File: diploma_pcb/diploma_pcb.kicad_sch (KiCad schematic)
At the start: 22 parts, among them Q1 2SC3356, Q3 2SC3356

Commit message: Divided in files, not made the showcase of the number
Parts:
- R1: value 2k -> 1k
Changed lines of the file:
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@@
 			)
 		)
-		(property "Value" "2k"
+		(property "Value" "1k"
 			(at 45.72 31.242 0)
 			(effects

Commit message: changes to ard, file button reader
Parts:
- Q1, Q3: footprint 2SC3356:SOT-23_MINIMOLD_REN -> 2SC3356:SOT-23_MINIMOLD_REN-M
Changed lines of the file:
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@@
 		)
 		(instances
-			(project ""
+			(project "diploma_pcb"
 				(path "/8eade999-89f4-4618-aeea-e9238b0bd165"
 					(reference "LED1")
@@
 			)
 		)
-		(property "Footprint" "2SC3356:SOT-23_MINIMOLD_REN"
+		(property "Footprint" "2SC3356:SOT-23_MINIMOLD_REN-M"
 			(at 48.895 62.865 0)
 			(effects
@@
 			)
 		)
-		(property "Footprint" "2SC3356:SOT-23_MINIMOLD_REN"
+		(property "Footprint" "2SC3356:SOT-23_MINIMOLD_REN-M"
 			(at 48.895 62.865 0)
 			(effects

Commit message: mods on PCB, Matplot, ?ard?
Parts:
- removed Q1, Q3: 2SC3356, 2SC3356:SOT-23_MINIMOLD_REN-M, symbol 2024-08-01_13-32-15:2SC3356
- removed R1: 1k, Resistor_SMD:R_1206_3216Metric, symbol Device:R
- removed R_3V3, R_5V1, R_div1, R_div2: R, Resistor_SMD:R_1206_3216Metric, symbol Device:R
- added C_oscilato1, C_supply1: .1uF, Capacitor_SMD:C_1206_3216Metric_Pad1.33x1.80mm_HandSolder, symbol Device:C
- added D1, D2: D_Schottky, symbol Device:D_Schottky
- added Q1: 2n3904, symbol Transistor_BJT:BC107
- added Rsch1: 1M, Resistor_SMD:R_1206_3216Metric, symbol Device:R
- R_gnd1, Rcc1: value 3k -> 4.7k
- Rf1: value 510к -> 680k
- Rg1: value 15к -> 10k
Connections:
- net Supply is gone; now on net 5V: 5_pins_op_amp1.5 (VDD), 8_pin_op_amp1.7 (V+), C1.1, C_GND1.2, Rcc1.1
- net 5V: now also D1.2 (A)
- net GND: now also C_supply1.1, Q1.2 (B)
- net Vout: now also A1.19 (A0)
- net at C104.1: now also Rsch1.2
- net at A1.14 (MOSI): now also C_oscilato1.2
- net 3.3V: no longer names the net of A1.17 (3V3)
- net signal renamed Signal
- new net: C_supply1.2, D1.1 (K), D2.1 (K), Q1.1 (E), Rsch1.1
- new net: C_oscilato1.1, D2.2 (A)
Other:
- note removed: "2SC3356"
- moved on the sheet: C104, C_GND1, R_gnd1, Rcc1

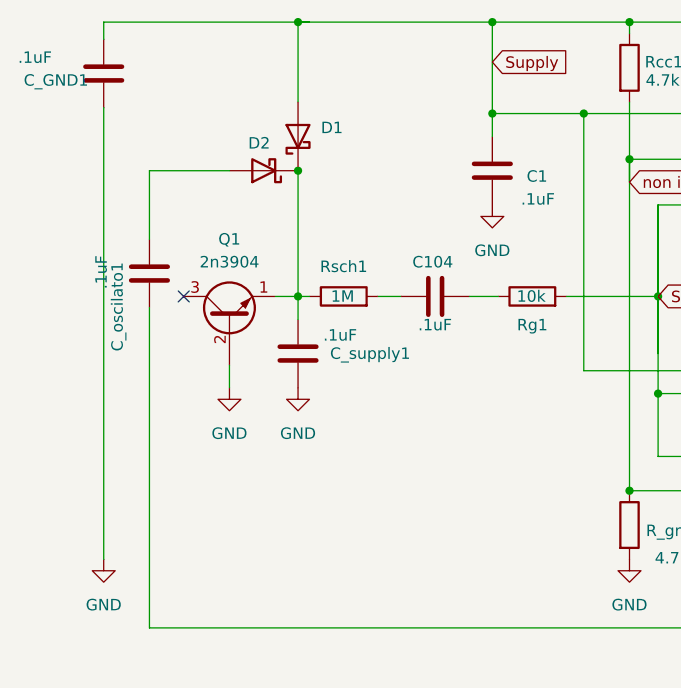
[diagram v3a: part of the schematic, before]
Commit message: PCB fixed Schottkey, Ard code with Union, GNU with bit save
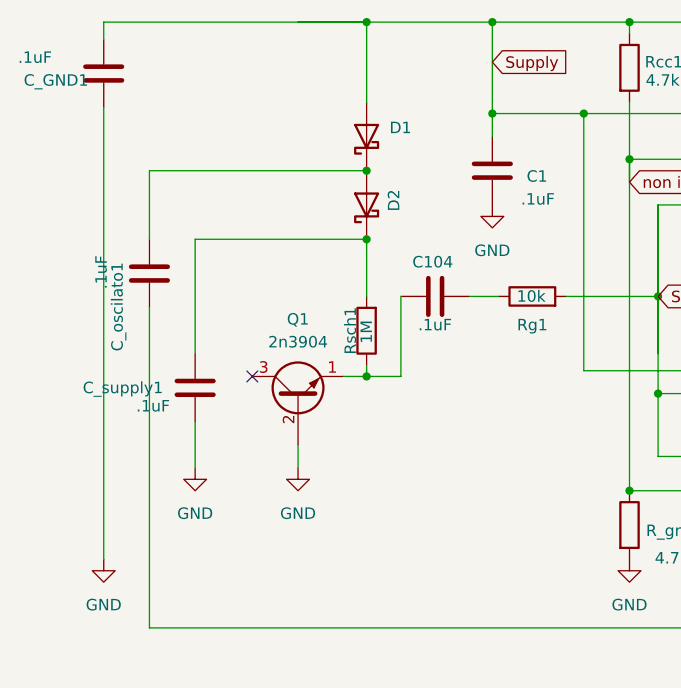
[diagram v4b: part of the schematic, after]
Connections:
- net GND: now also C_supply1.2; no longer C_supply1.1
- net at C104.1: now also Q1.1 (E), Rsch1.1; no longer Rsch1.2
- net at C_oscilato1.1, D2.2 (A): now also D1.1 (K)
- new net: C_supply1.1, D2.1 (K), Rsch1.2
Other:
- moved on the sheet: C_supply1, D1, D2, Q1, Rsch1

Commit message: Schematic, GNU, matplot, Ard code - Done
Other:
- moved on the sheet: C_GND1
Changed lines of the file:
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@@
 	)
 	(junction
-		(at 45.72 30.48)
+		(at 171.45 13.97)
 		(diameter 0)
 		(color 0 0 0 0)
 	)
 	(junction
-		(at 74.93 13.97)
+		(at 45.72 30.48)
 		(diameter 0)
 		(color 0 0 0 0)
 	)
 	(junction
-		(at 59.69 13.97)
+		(at 74.93 13.97)
 		(diameter 0)
 		(color 0 0 0 0)
 	)
 	(junction
-		(at 45.72 13.97)
+		(at 59.69 13.97)
 		(diameter 0)
 		(color 0 0 0 0)
@@
 	(wire
 		(pts
-			(xy 16.51 13.97) (xy 45.72 13.97)
+			(xy 193.04 13.97) (xy 171.45 13.97)
 		)
 		(stroke
@@
 	(wire
 		(pts
-			(xy 16.51 15.875) (xy 16.51 13.97)
+			(xy 193.04 17.78) (xy 193.04 13.97)
 		)
 		(stroke
@@
 	(wire
 		(pts
-			(xy 38.1 13.97) (xy 45.72 13.97)
-		)
-		(stroke
-			(width 0)
-			(type default)
-		)
-	)
-	(wire
-		(pts
 			(xy 57.15 44.45) (xy 60.325 44.45)
 		)
@@
 	(wire
 		(pts
-			(xy 59.69 13.97) (xy 74.93 13.97)
-		)
-		(stroke
-			(width 0)
-			(type default)
-			(color 255 0 0 1)
-		)
-	)
-	(wire
-		(pts
 			(xy 45.72 52.07) (xy 45.72 53.34)
 		)
@@
 	(wire
 		(pts
+			(xy 74.93 13.97) (xy 59.69 13.97)
+		)
+		(stroke
+			(width 0)
+			(type default)
+			(color 255 0 0 1)
+		)
+	)
+	(wire
+		(pts
 			(xy 78.105 34.29) (xy 78.105 44.45)
 		)
@@
 			(width 0)
 			(type default)
+			(color 255 0 0 1)
 		)
 	)
@@
 	(wire
 		(pts
-			(xy 16.51 23.495) (xy 16.51 73.66)
+			(xy 193.04 25.4) (xy 193.04 26.035)
 		)
 		(stroke
@@
 	(symbol
 		(lib_id "Device:C")
-		(at 16.51 19.685 180)
+		(at 193.04 21.59 180)
 		(unit 1)
 		(exclude_from_sim no)
@@
 		(dnp no)
 		(property "Reference" "C_GND1"
-			(at 7.62 20.447 0)
+			(at 184.15 22.352 0)
 			(effects
 				(font
@@
 		)
 		(property "Value" ".1uF"
-			(at 6.985 17.907 0)
+			(at 183.515 19.812 0)
 			(effects
 				(font
@@
 		)
 		(property "Footprint" "Capacitor_SMD:C_1206_3216Metric_Pad1.33x1.80mm_HandSolder"
-			(at 15.5448 15.875 0)
+			(at 192.0748 17.78 0)
 			(effects
 				(font
@@
 		)
 		(property "Datasheet" "~"
-			(at 16.51 19.685 0)
+			(at 193.04 21.59 0)
 			(effects
 				(font
@@
 		)
 		(property "Description" "Unpolarized capacitor"
-			(at 16.51 19.685 0)
+			(at 193.04 21.59 0)
 			(effects
 				(font
@@
 	(symbol
 		(lib_id "power:GND")
-		(at 16.51 73.66 0)
+		(at 193.04 26.035 0)
 		(unit 1)
 		(exclude_from_sim no)
@@
 		(fields_autoplaced yes)
 		(property "Reference" "#PWR01"
-			(at 16.51 80.01 0)
+			(at 193.04 32.385 0)
 			(effects
 				(font
@@
 		)
 		(property "Value" "GND"
-			(at 16.51 78.74 0)
+			(at 193.04 31.115 0)
 			(effects
 				(font
@@
 		)
 		(property "Footprint" ""
-			(at 16.51 73.66 0)
+			(at 193.04 26.035 0)
 			(effects
 				(font
@@
 		)
 		(property "Datasheet" ""
-			(at 16.51 73.66 0)
+			(at 193.04 26.035 0)
 			(effects
 				(font
@@
 		)
 		(property "Description" "Power symbol creates a global label with name \"GND\" , ground"
-			(at 16.51 73.66 0)
+			(at 193.04 26.035 0)
 			(effects
 				(font

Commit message: Daemon created, Footprint Assigned, Device constatnly sending
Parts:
- removed Q1: 2n3904, symbol Transistor_BJT:BC107
- added Q2: 2n3904, Package_TO_SOT_SMD:SOT-23, symbol Transistor_BJT:MMBTA44
- D1, D2: footprint (none) -> Diode_SMD:D_1812_4532Metric_Pad1.30x3.40mm_HandSolder
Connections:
- net GND: now also Q2.1 (B)
- net at C104.1, Rsch1.1: now also Q2.2 (E)
- net at A1.14 (MOSI): no longer C_oscilato1.2
- net at A1.6 (D3): now also C_oscilato1.2
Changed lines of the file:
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@@
 	)
 	(no_connect
-		(at 153.67 36.83)
+		(at 153.67 59.69)
 	)
 	(no_connect
@@
 	(wire
 		(pts
-			(xy 38.1 60.96) (xy 38.1 63.5)
-		)
-		(stroke
-			(width 0)
-			(type default)
-		)
-	)
-	(wire
-		(pts
 			(xy 74.93 13.97) (xy 74.93 15.24)
 		)
@@
 	(wire
 		(pts
-			(xy 69.85 52.705) (xy 81.28 52.705)
+			(xy 124.46 36.83) (xy 153.67 36.83)
 		)
 		(stroke
 			(width 0)
 			(type default)
-			(color 255 0 0 1)
 		)
 	)
 	(wire
 		(pts
-			(xy 45.72 52.07) (xy 45.72 53.34)
+			(xy 69.85 52.705) (xy 81.28 52.705)
 		)
 		(stroke
 			(width 0)
 			(type default)
+			(color 255 0 0 1)
 		)
 	)
 	(wire
 		(pts
-			(xy 74.93 29.21) (xy 86.36 29.21)
+			(xy 45.72 52.07) (xy 45.72 53.34)
 		)
 		(stroke
 			(width 0)
 			(type default)
-			(color 0 0 255 1)
 		)
 	)
 	(wire
 		(pts
-			(xy 167.64 74.295) (xy 162.56 74.295)
+			(xy 74.93 29.21) (xy 86.36 29.21)
 		)
 		(stroke
 			(width 0)
 			(type default)
+			(color 0 0 255 1)
 		)
 	)
 	(wire
 		(pts
-			(xy 129.54 59.69) (xy 153.67 59.69)
+			(xy 167.64 74.295) (xy 162.56 74.295)
 		)
 		(stroke
@@
 	(wire
 		(pts
-			(xy 129.54 81.28) (xy 21.59 81.28)
+			(xy 124.46 81.28) (xy 21.59 81.28)
 		)
 		(stroke
@@
 	(wire
 		(pts
-			(xy 129.54 59.69) (xy 129.54 81.28)
+			(xy 124.46 36.83) (xy 124.46 81.28)
 		)
 		(stroke
@@
 			)
 		)
-		(property "Footprint" ""
+		(property "Footprint" "Diode_SMD:D_1812_4532Metric_Pad1.30x3.40mm_HandSolder"
 			(at 45.72 34.29 0)
 			(effects
@@
 	)
 	(symbol
-		(lib_id "Transistor_BJT:BC107")
-		(at 38.1 55.88 90)
-		(unit 1)
-		(exclude_from_sim no)
-		(in_bom yes)
-		(on_board yes)
-		(dnp no)
-		(fields_autoplaced yes)
-		(property "Reference" "Q1"
-			(at 38.1 46.99 90)
-			(effects
-				(font
-					(size 1.27 1.27)
-				)
-			)
-		)
-		(property "Value" "2n3904"
-			(at 38.1 49.53 90)
-			(effects
-				(font
-					(size 1.27 1.27)
-				)
-			)
-		)
-		(property "Footprint" ""
-			(at 40.005 50.8 0)
-			(effects
-				(font
-					(size 1.27 1.27)
-					(italic yes)
-				)
-				(justify left)
-				(hide yes)
-			)
-		)
-		(property "Datasheet" "http://www.b-kainka.de/Daten/Transistor/BC108.pdf"
-			(at 38.1 55.88 0)
-			(effects
-				(font
-					(size 1.27 1.27)
-				)
-				(justify left)
-				(hide yes)
-			)
-		)
-		(property "Description" "0.1A Ic, 50V Vce, Low Noise General Purpose NPN Transistor, TO-18"
-			(at 38.1 55.88 0)
-			(effects
-				(font
-					(size 1.27 1.27)
-				)
-				(hide yes)
-			)
-		)
-		(pin "3"
-		)
-		(pin "1"
-		)
-		(pin "2"
-		)
-		(instances
-			(project ""
-				(path "/8eade999-89f4-4618-aeea-e9238b0bd165"
-					(reference "Q1")
-					(unit 1)
-				)
-			)
-		)
-	)
-	(symbol
 		(lib_id "Device:R")
 		(at 149.86 52.07 270)
@@
 	(symbol
 		(lib_id "power:GND")
-		(at 38.1 63.5 0)
+		(at 38.1 60.96 0)
 		(unit 1)
 		(exclude_from_sim no)
@@
 		(fields_autoplaced yes)
 		(property "Reference" "#PWR08"
-			(at 38.1 69.85 0)
+			(at 38.1 67.31 0)
 			(effects
 				(font
@@
 		)
 		(property "Value" "GND"
-			(at 38.1 68.58 0)
+			(at 38.1 66.04 0)
 			(effects
 				(font
@@
 		)
 		(property "Footprint" ""
-			(at 38.1 63.5 0)
+			(at 38.1 60.96 0)
 			(effects
 				(font
@@
 		)
 		(property "Datasheet" ""
-			(at 38.1 63.5 0)
+			(at 38.1 60.96 0)
 			(effects
 				(font
@@
 		)
 		(property "Description" "Power symbol creates a global label with name \"GND\" , ground"
-			(at 38.1 63.5 0)
+			(at 38.1 60.96 0)
 			(effects
 				(font
@@
 			)
 		)
-		(property "Footprint" ""
+		(property "Footprint" "Diode_SMD:D_1812_4532Metric_Pad1.30x3.40mm_HandSolder"
 			(at 45.72 26.67 0)
 			(effects
@@
 					(unit 1)
 				)
+			)
+		)
+	)
+	(symbol
+		(lib_id "Transistor_BJT:MMBTA44")
+		(at 38.1 55.88 90)
+		(unit 1)
+		(exclude_from_sim no)
+		(in_bom yes)
+		(on_board yes)
+		(dnp no)
+		(fields_autoplaced yes)
+		(property "Reference" "Q2"
+			(at 38.1 46.99 90)
+			(effects
+				(font
+					(size 1.27 1.27)
+				)
+			)
+		)
+		(property "Value" "2n3904"
+			(at 38.1 49.53 90)
+			(effects
+				(font
+					(size 1.27 1.27)
+				)
+			)
+		)
+		(property "Footprint" "Package_TO_SOT_SMD:SOT-23"
+			(at 40.005 50.8 0)
+			(effects
+				(font
+					(size 1.27 1.27)
+					(italic yes)
+				)
+				(justify left)
+				(hide yes)
+			)
+		)
+		(property "Datasheet" "https://diotec.com/request/datasheet/mmbta42.pdf"
+			(at 38.1 55.88 0)
+			(effects
+				(font
+					(size 1.27 1.27)
+				)
+				(justify left)
+				(hide yes)
+			)
+		)
+		(property "Description" "0.3A Ic, 400V Vce, NPN High Voltage Transistor, SOT-23"
+			(at 38.1 55.88 0)
+			(effects
+				(font
+					(size 1.27 1.27)
+				)
+				(hide yes)
+			)
+		)
+		(pin "2"
+		)
+		(pin "1"
+		)
+		(pin "3"
+		)
+		(instances
+			(project ""
+				(path "/8eade999-89f4-4618-aeea-e9238b0bd165"
+					(reference "Q2")
+					(unit 1)
+				)

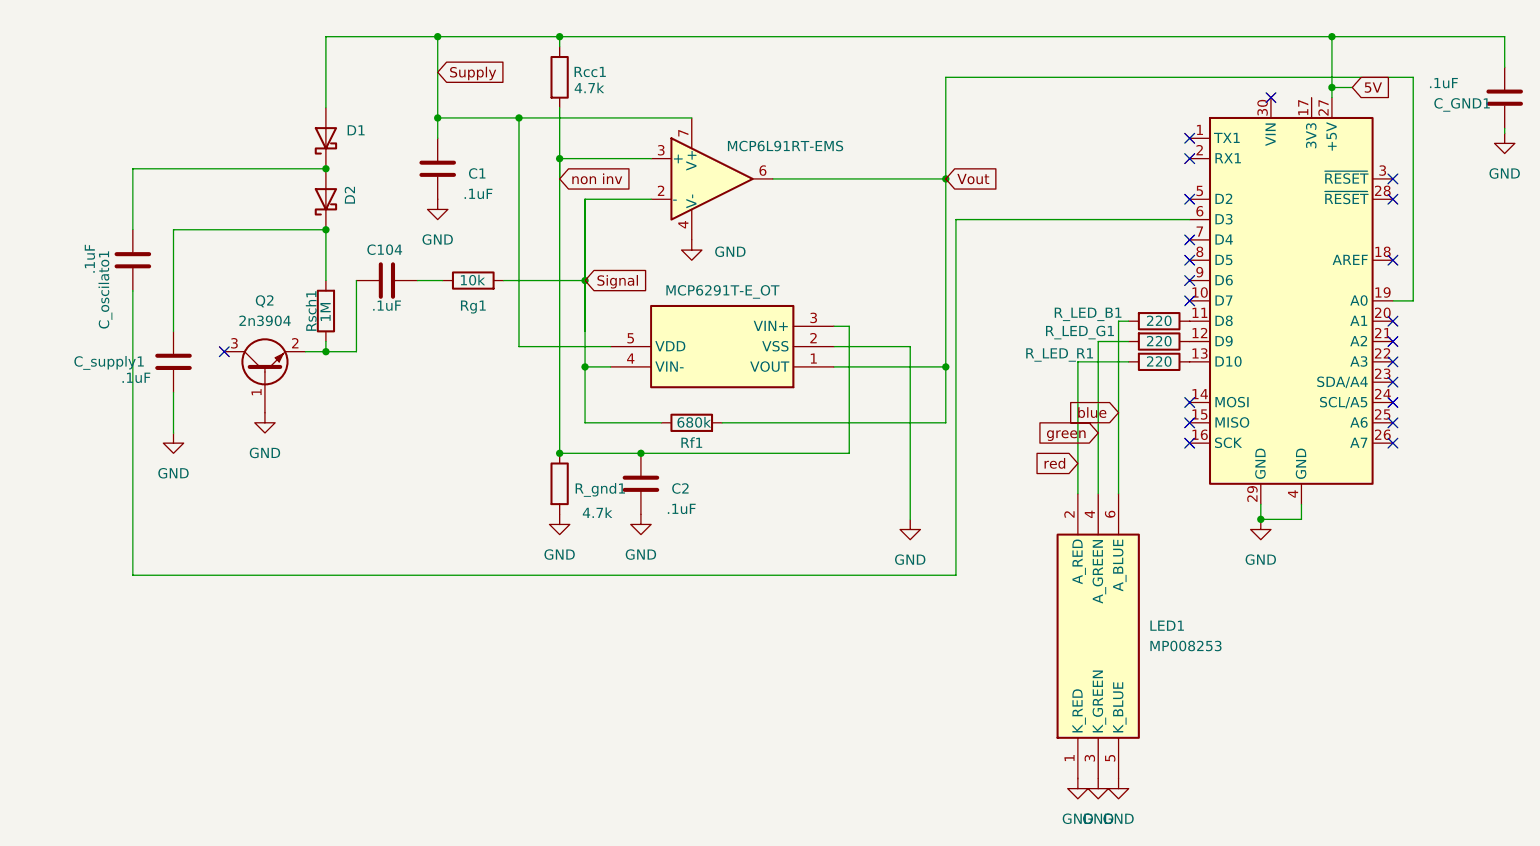
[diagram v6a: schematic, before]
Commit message: PCB created (not checked), ard changes?, Footprints set up
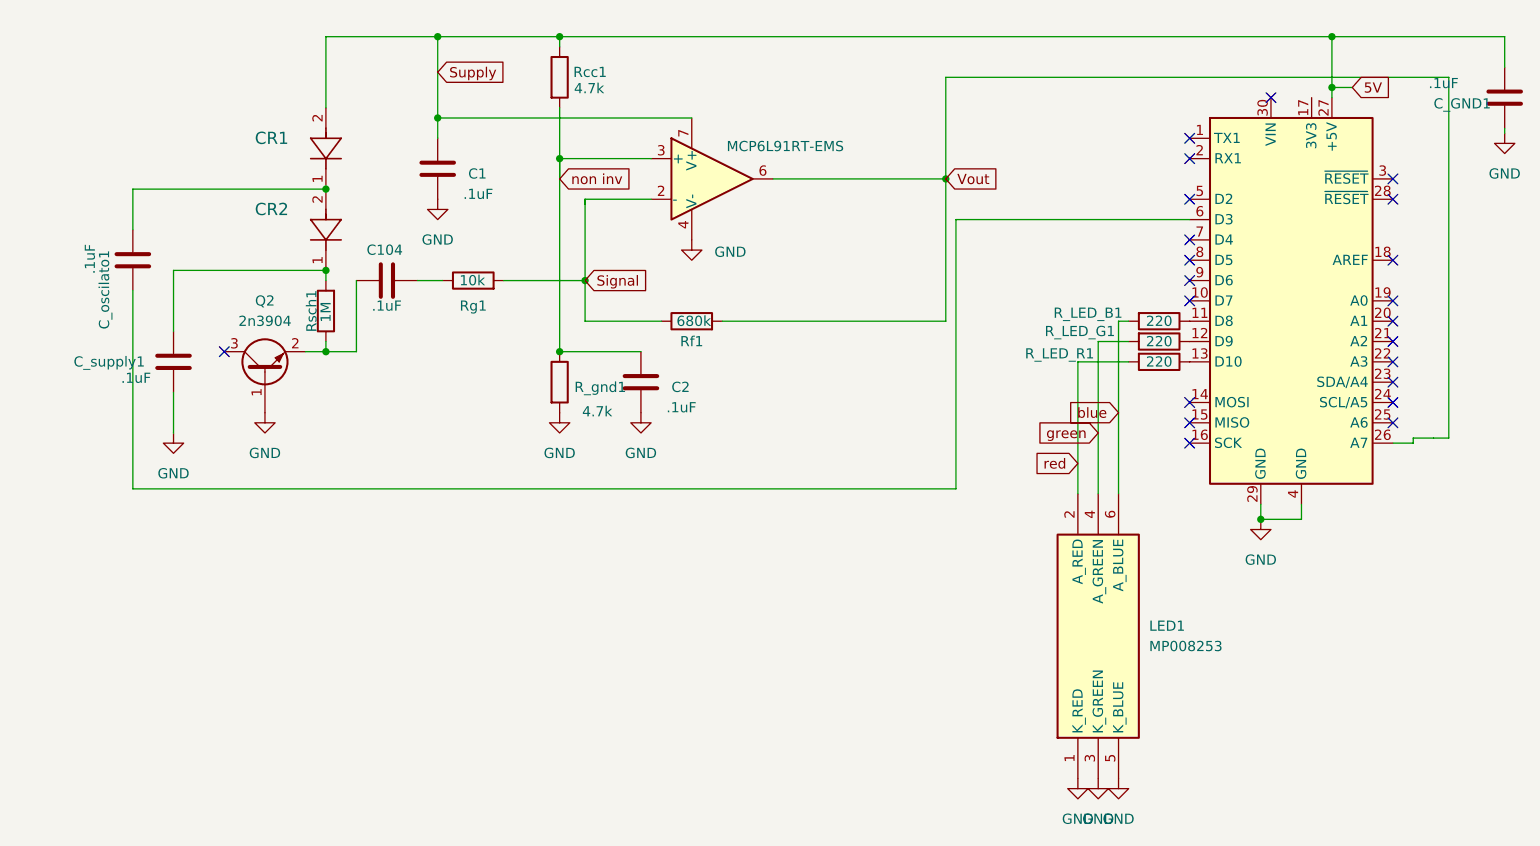
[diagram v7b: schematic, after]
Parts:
- removed 5_pins_op_amp1: MCP6291T-E_OT, op_amp_MCP6291T-E/OT:SOT95P280X145-5N, symbol MCP6291T-E_OT:MCP6291T-E_OT
- removed D1, D2: D_Schottky, Diode_SMD:D_1812_4532Metric_Pad1.30x3.40mm_HandSolder, symbol Device:D_Schottky
- added CR1, CR2: MBRS1100T3G, MBRS1100T3G:SMB_403A-03_ONS, symbol MBRS1100T3G:MBRS1100T3G
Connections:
- net 5V: now also CR1.2
- net Vout: now also A1.26 (A7); no longer A1.19 (A0)
- net at C_supply1.1, Rsch1.2: now also CR2.1
- net at C_oscilato1.1: now also CR1.1, CR2.2
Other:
- moved on the sheet: C2, R_gnd1, Rf1
